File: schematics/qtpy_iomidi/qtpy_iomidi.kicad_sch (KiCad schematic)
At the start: 21 parts, among them J1 AudioJack4, J2 AudioJack4, J3 USB_A, J4 Conn_01x02_Pin, U2 H11L1

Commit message: some silkscreen
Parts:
- added LED1: LED, LED_SMD:LED_0805_2012Metric, symbol Device:LED
- added R8: 1k, Resistor_SMD:R_0805_2012Metric, symbol Device:R
- renumbered D2 to LED2, D3 to LED3
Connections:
- net +3V3: now also R8.2
- net LED: now reaches U1.SCK
- net LED: now also LED1.1 (K)
- new net: LED1.2 (A), R8.1

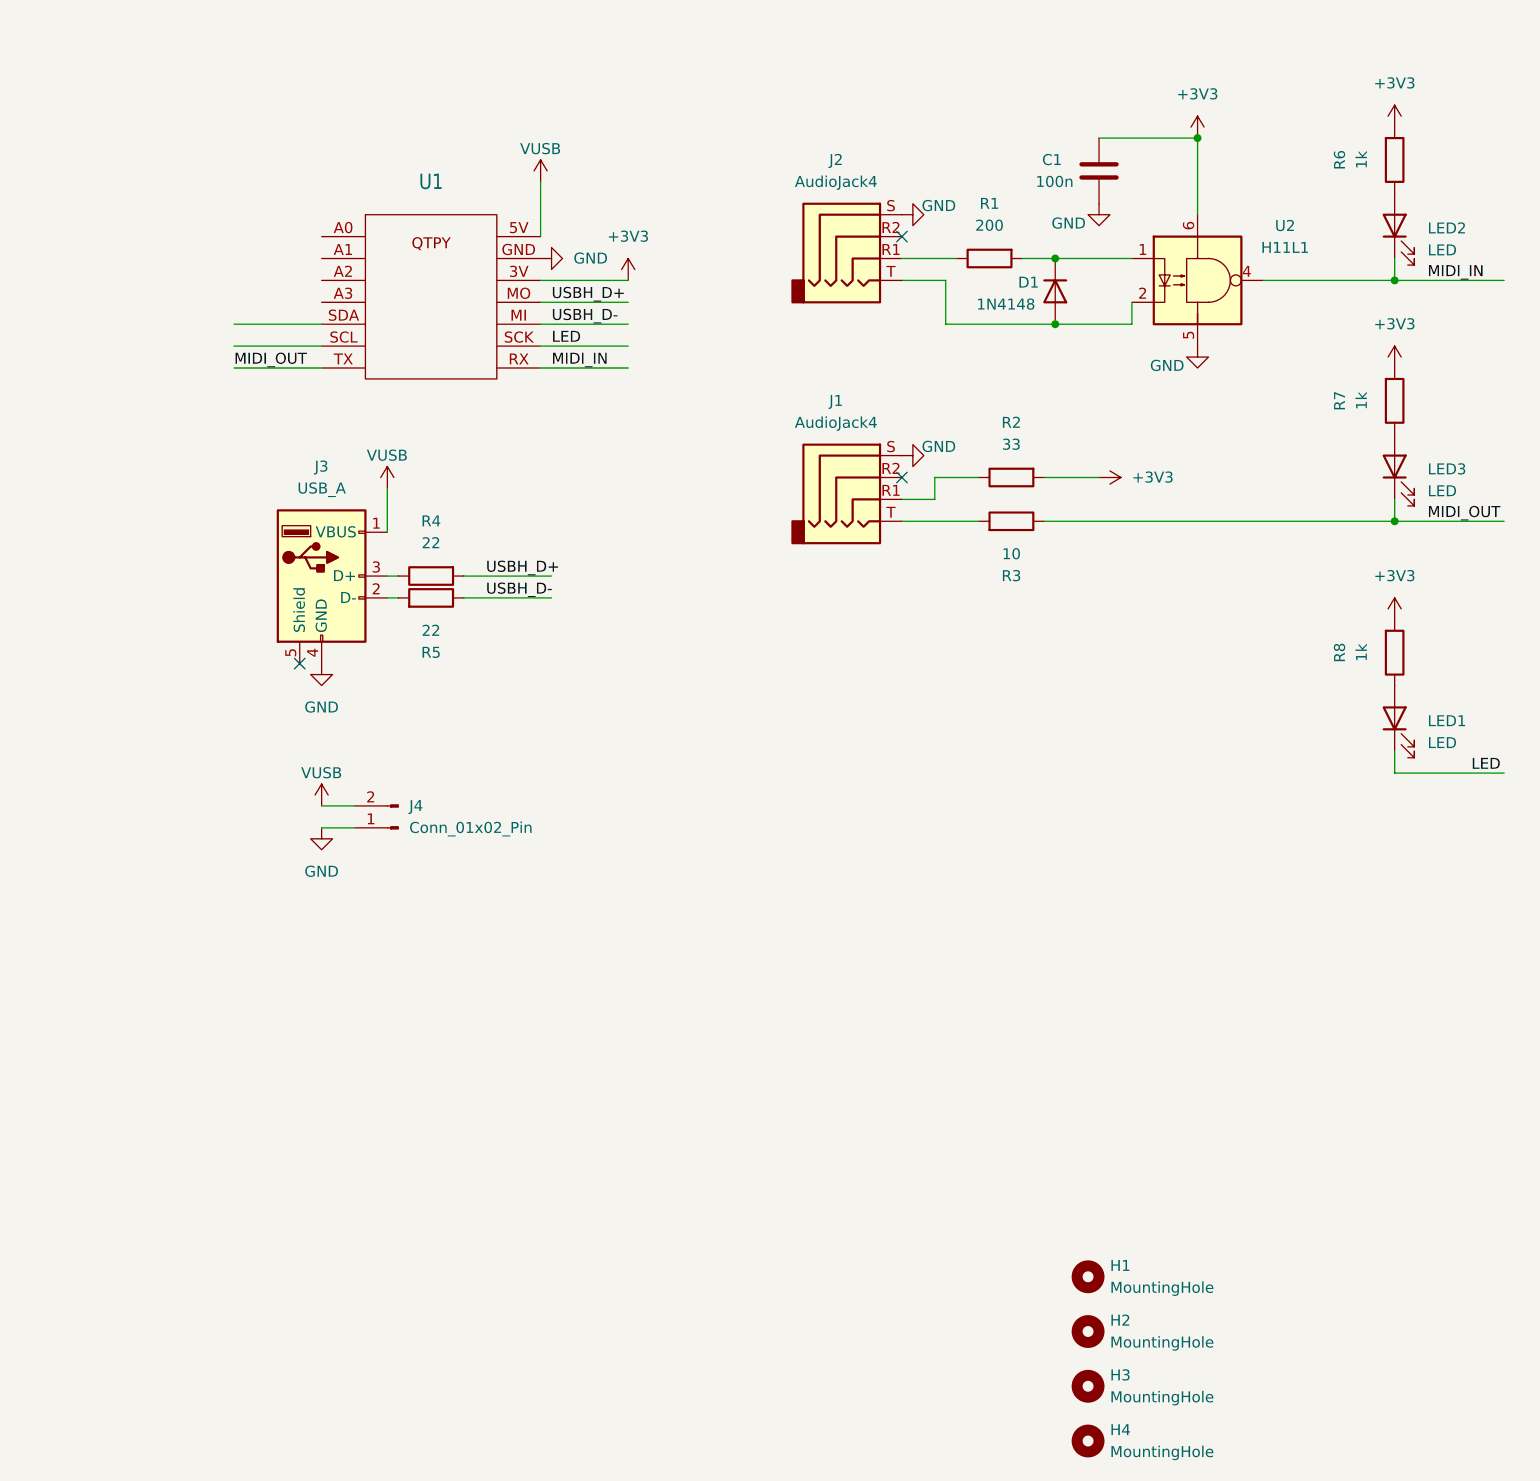
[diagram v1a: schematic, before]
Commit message: switch to LCSC USB SMD host jack, add display & switch
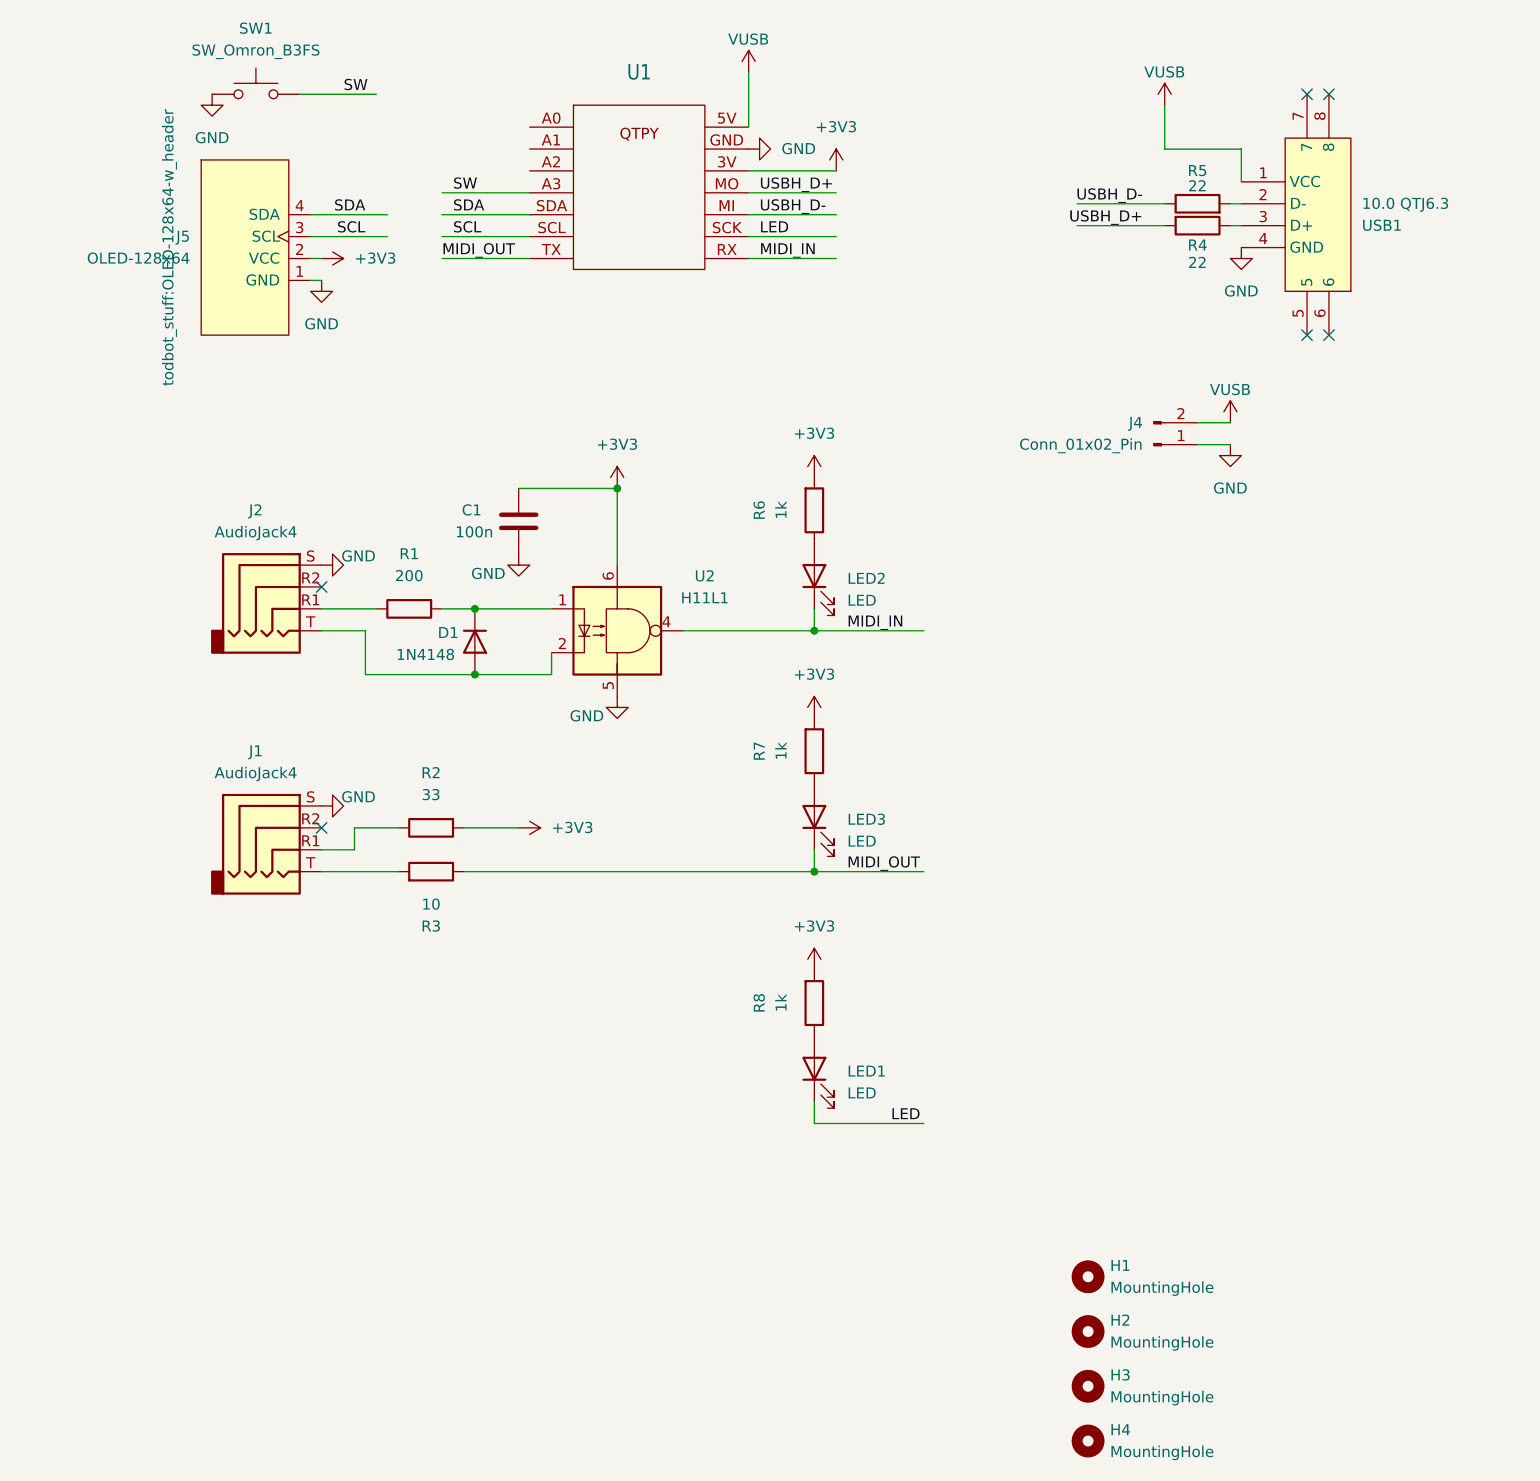
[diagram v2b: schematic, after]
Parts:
- removed J3: USB_A, Connector_USB:USB_A_Receptacle_GCT_USB1046, symbol Connector:USB_A
- added J5: OLED-128x64, todbot_stuff:OLED-128x64-w_header, symbol kleeb_display:OLED-128x64
- added SW1: SW_Omron_B3FS, Button_Switch_THT:SW_PUSH_6mm_H4.3mm, symbol Switch:SW_Omron_B3FS
- added USB1: 10.0 QTJ6.3, easyeda2kicad:USB-A-SMD_10.0-QTJ6.3, symbol easyeda2kicad:10.0QTJ6.3
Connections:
- net +3V3: now also J5.2 (VCC)
- net GND: now also J5.1 (GND), SW1.1, USB1.4 (GND)
- net VUSB: now also USB1.1 (VCC)
- net SW: now reaches U1.A3
- net SW: now also SW1.2
- net SCL: now reaches U1.SCL
- net SCL: now also J5.3 (SCL)
- net SDA: now reaches U1.SDA
- net SDA: now also J5.4 (SDA)
- net at R5.2: now also USB1.2 (D-)
- net at R4.1: now also USB1.3 (D+)
- no-connect marks 3 -> 6
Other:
- moved on the sheet: C1, D1, J1, J2, J4, LED1, LED2, LED3, R1, R2, R3, R4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

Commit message: more pcb tweaking
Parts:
- U1: footprint todbot_eagle2023:QTPY_TH -> todbot_eagle2023:QTPY_TH_HEADERSOCKET
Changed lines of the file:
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@@
 			)
 		)
-		(property "Footprint" "todbot_eagle2023:QTPY_TH"
+		(property "Footprint" "todbot_eagle2023:QTPY_TH_HEADERSOCKET"
 			(at 95.504 53.34 0)
 			(effects

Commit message: added encoder
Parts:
- added SW2: RotaryEncoder_Switch, Rotary_Encoder:RotaryEncoder_Alps_EC11E-Switch_Vertical_H20mm_CircularMountingHoles, symbol Device:RotaryEncoder_Switch
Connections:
- net GND: now also SW2.C, SW2.S2
- net ENC_A: now reaches U1.A0
- net ENC_A: now also SW2.A
- net ENC_B: now reaches U1.A1 (9)
- net ENC_B: now also SW2.B
- net ENC_SW: now reaches U1.A2
- net ENC_SW: now also SW2.S1
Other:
- moved on the sheet: C1, D1, J1, J2, J5, LED1, LED2, LED3, R1, R2, R3, R6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

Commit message: qtpy holes too small, fixed I think
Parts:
- J1, J2: LCSC (none) -> C431535
- LED1, LED2, LED3: LCSC (none) -> C49678
- U2: LCSC (none) -> C78589
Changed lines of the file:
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@@
+			)
+		)
+		(property "LCSC" "C431535"
+			(at 48.26 149.86 0)
+			(effects
+				(font
+					(size 1.27 1.27)
+				)
+				(hide yes)
 			)
 		)
@@
 			)
 		)
+		(property "LCSC" "C431535"
+			(at 48.26 121.92 0)
+			(effects
+				(font
+					(size 1.27 1.27)
+				)
+				(hide yes)
+			)
+		)
 		(pin "R2"
 		)
@@
 			)
 		)
+		(property "LCSC" "C78589"
+			(at 87.63 127 0)
+			(effects
+				(font
+					(size 1.27 1.27)
+				)
+				(hide yes)
+			)
+		)
 		(pin "5"
 		)
@@
 			)
 		)
-		(property "Description" "Light emitting diode"
+		(property "Description" "Light emitting diode, green"
 			(at 110.49 120.65 0)
+			(effects
+				(font
+					(size 1.27 1.27)
+				)
+				(hide yes)
+			)
+		)
+		(property "LCSC" "C49678"
+			(at 110.49 120.65 90)
 			(effects
 				(font
@@
 			)
 		)
-		(property "Description" "Light emitting diode"
+		(property "Description" "Light emitting diode, green"
 			(at 110.49 148.59 0)
+			(effects
+				(font
+					(size 1.27 1.27)
+				)
+				(hide yes)
+			)
+		)
+		(property "LCSC" "C49678"
+			(at 110.49 148.59 90)
 			(effects
 				(font
@@
 			)
 		)
-		(property "Description" "Light emitting diode"
+		(property "Description" "Light emitting diode, green"
 			(at 110.49 177.8 0)
 			(effects
 				(font
+					(size 1.27 1.27)
+				)
+				(hide yes)
+			)
+		)
+		(property "LCSC" "C49678"
+			(at 110.49 177.8 90)
+			(effects
+				(font
